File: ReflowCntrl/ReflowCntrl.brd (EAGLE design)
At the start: 86 x 50.8 mm, 13 parts, among them J1 DCJ0202, T1 2N2222, X1 1751248

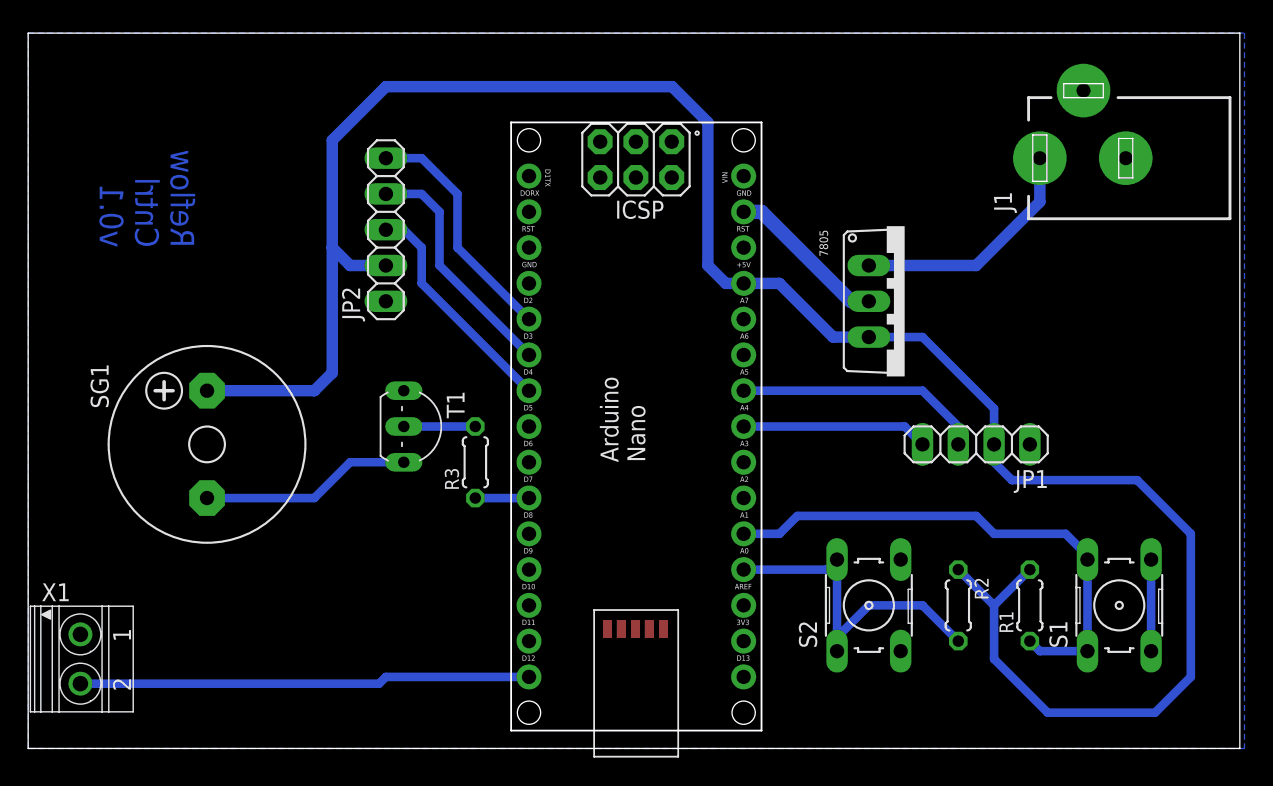
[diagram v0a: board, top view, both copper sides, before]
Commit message: Changed dimension boundry in Arduino Nano library to be tPlace instead to allow gnd plane to flow properly.
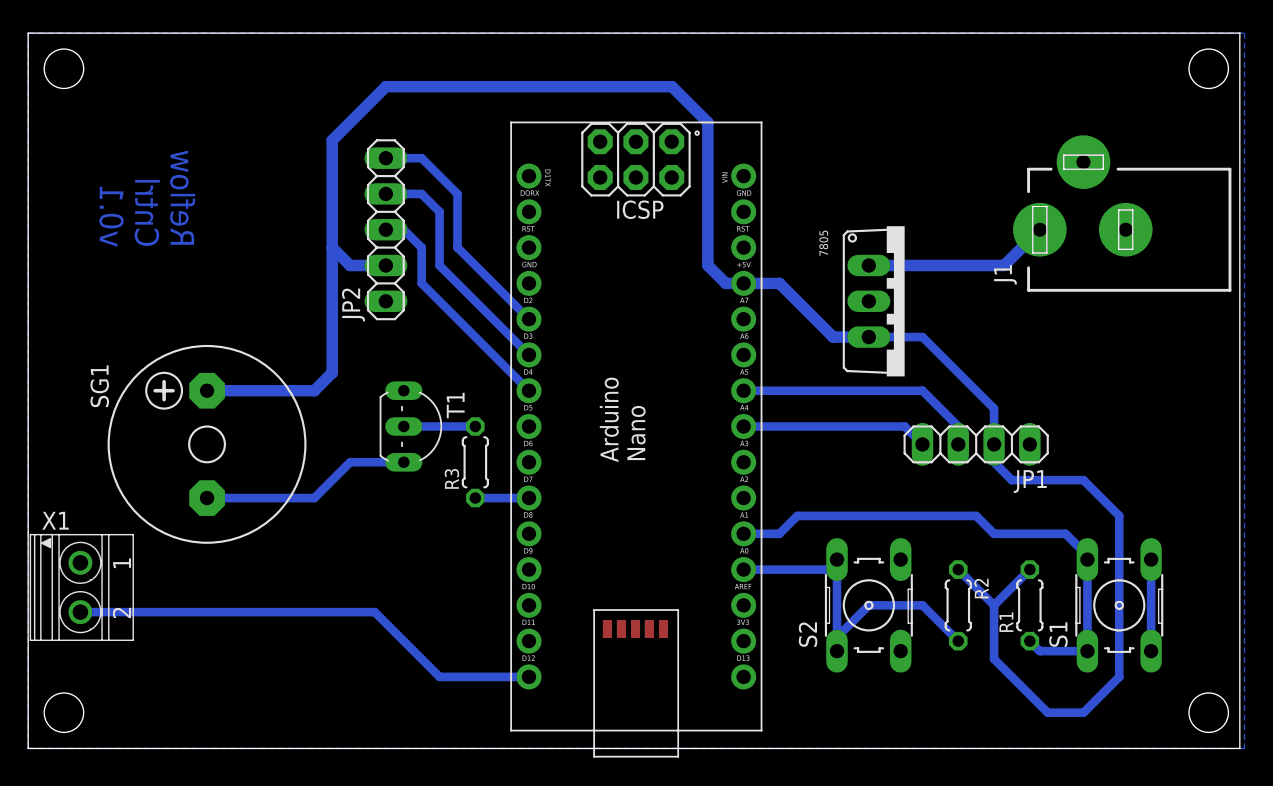
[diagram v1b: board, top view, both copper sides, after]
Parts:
- moved X1 5.08 mm to (3.81, 11.4)
- moved J1 5.08 mm to (74.9, 36.8)
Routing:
- net GND: track 18.0 -> 6.50 mm
- net VCC: track 151.9 -> 142.5 mm
- net N$5: track 17.1 -> 13.2 mm
- net SSR: track 32.0 -> 33.8 mm

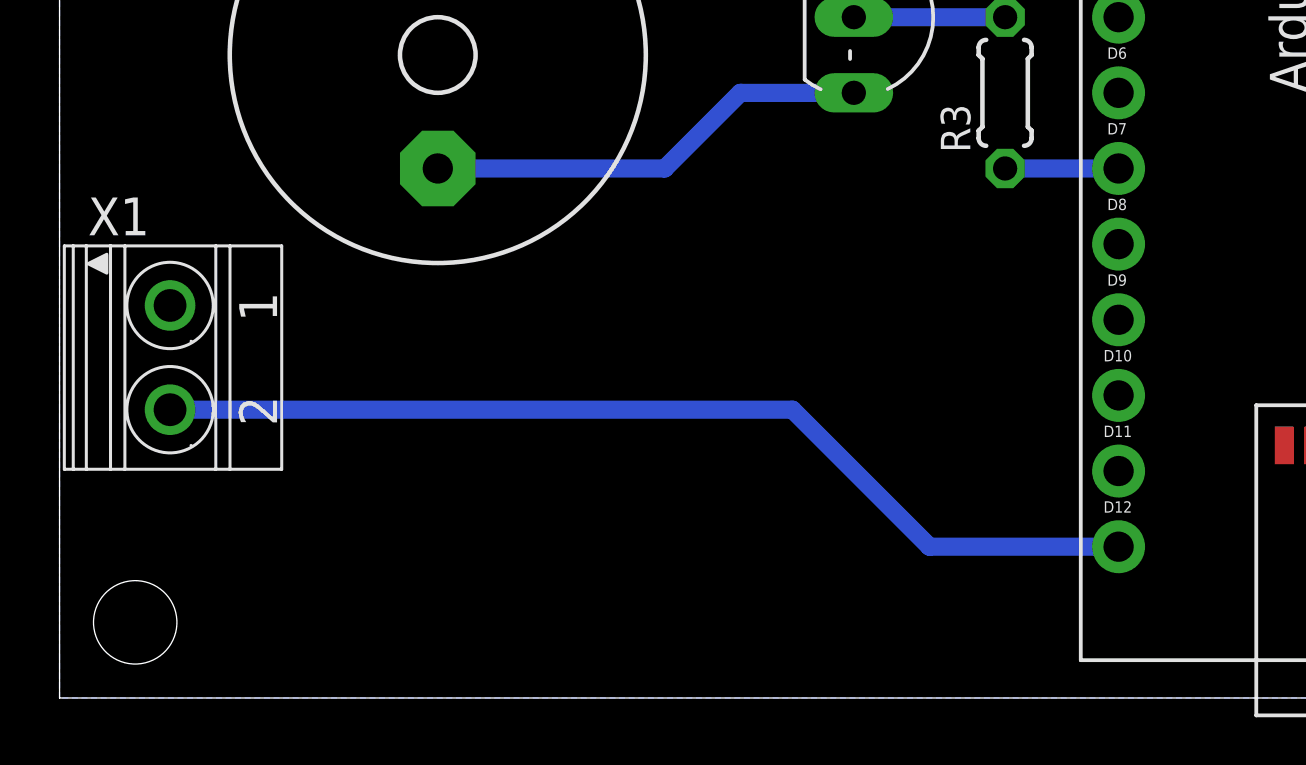
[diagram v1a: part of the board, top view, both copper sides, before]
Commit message: Change SSR terminal to Wago part.
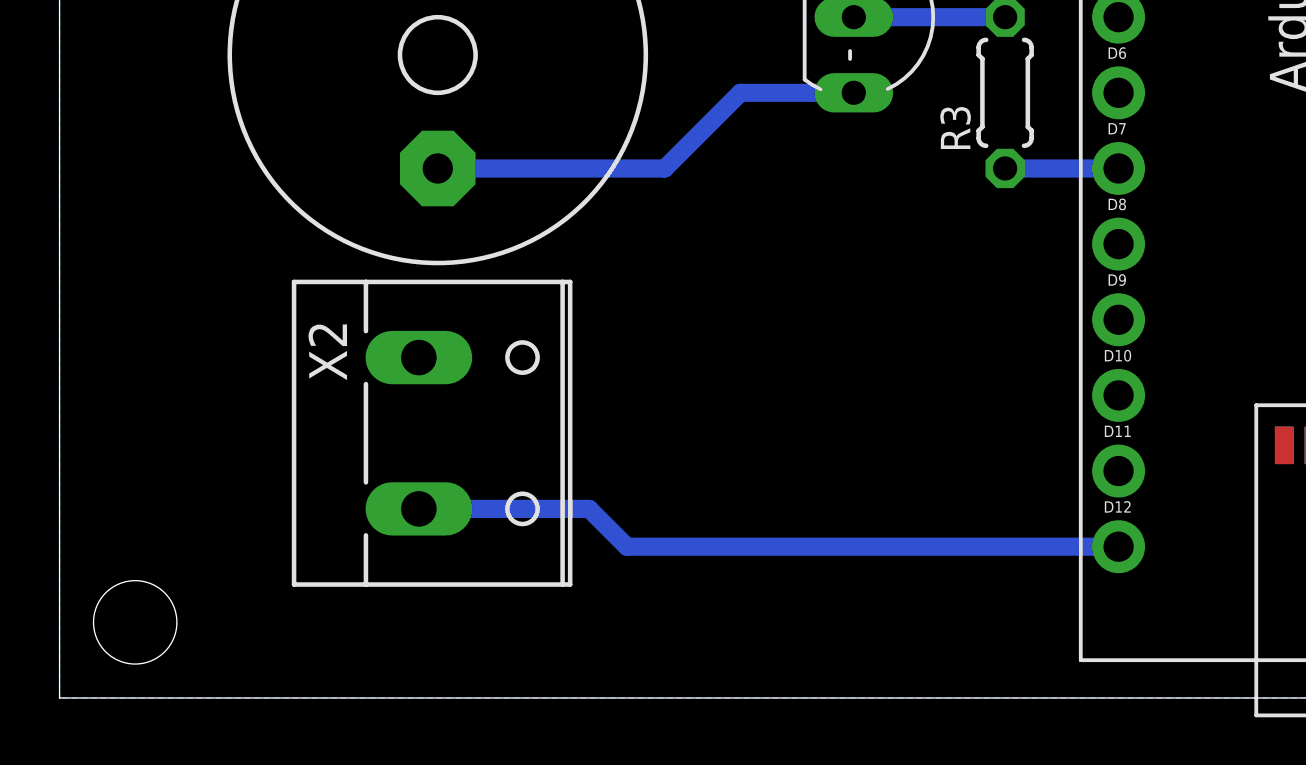
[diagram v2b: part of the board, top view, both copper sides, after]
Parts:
- removed X1: 1751248, con-phoenix-350:1751248
- added X2: (no value), con-wago-508:W237-132
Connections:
- net GND: now also X2.1; no longer X1.1
- net SSR: now also X2.2; no longer X1.2
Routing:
- net SSR: track 33.8 -> 24.0 mm

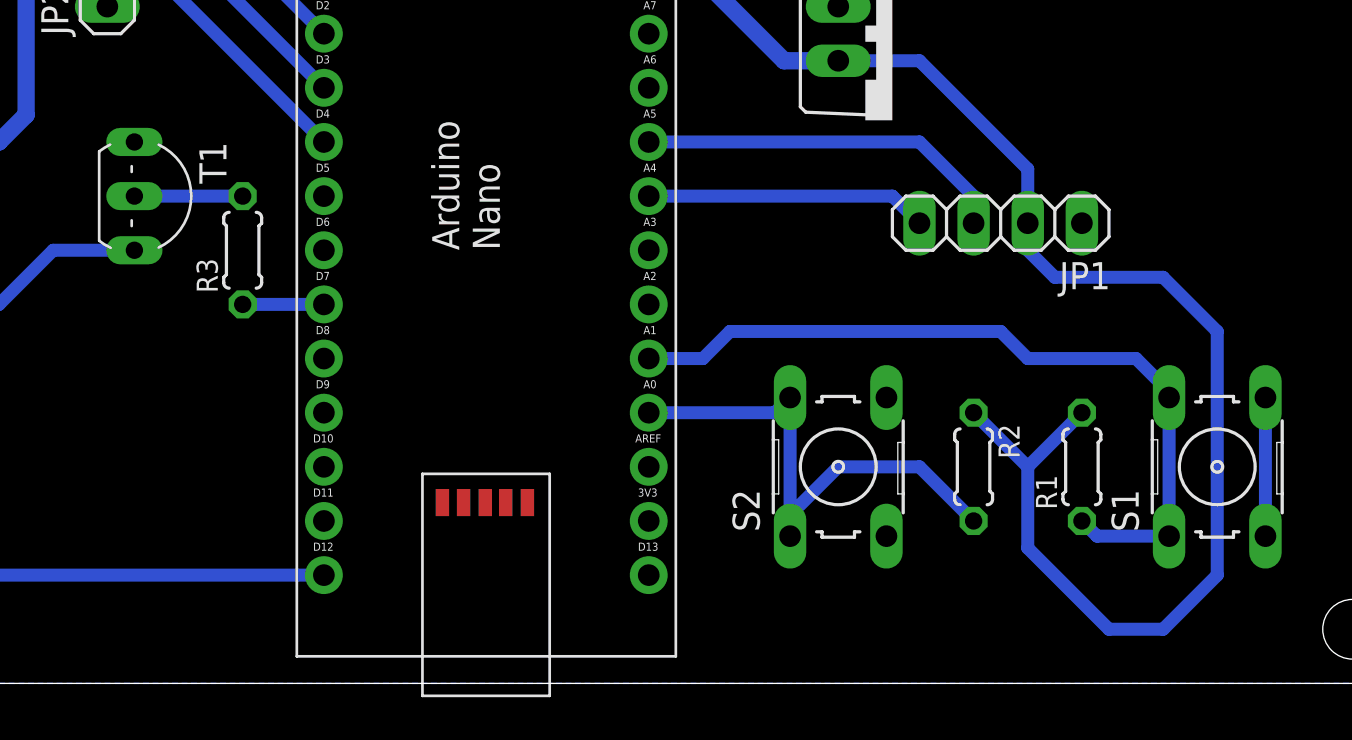
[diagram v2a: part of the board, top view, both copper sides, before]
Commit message: Change resistors to 0207/10 package
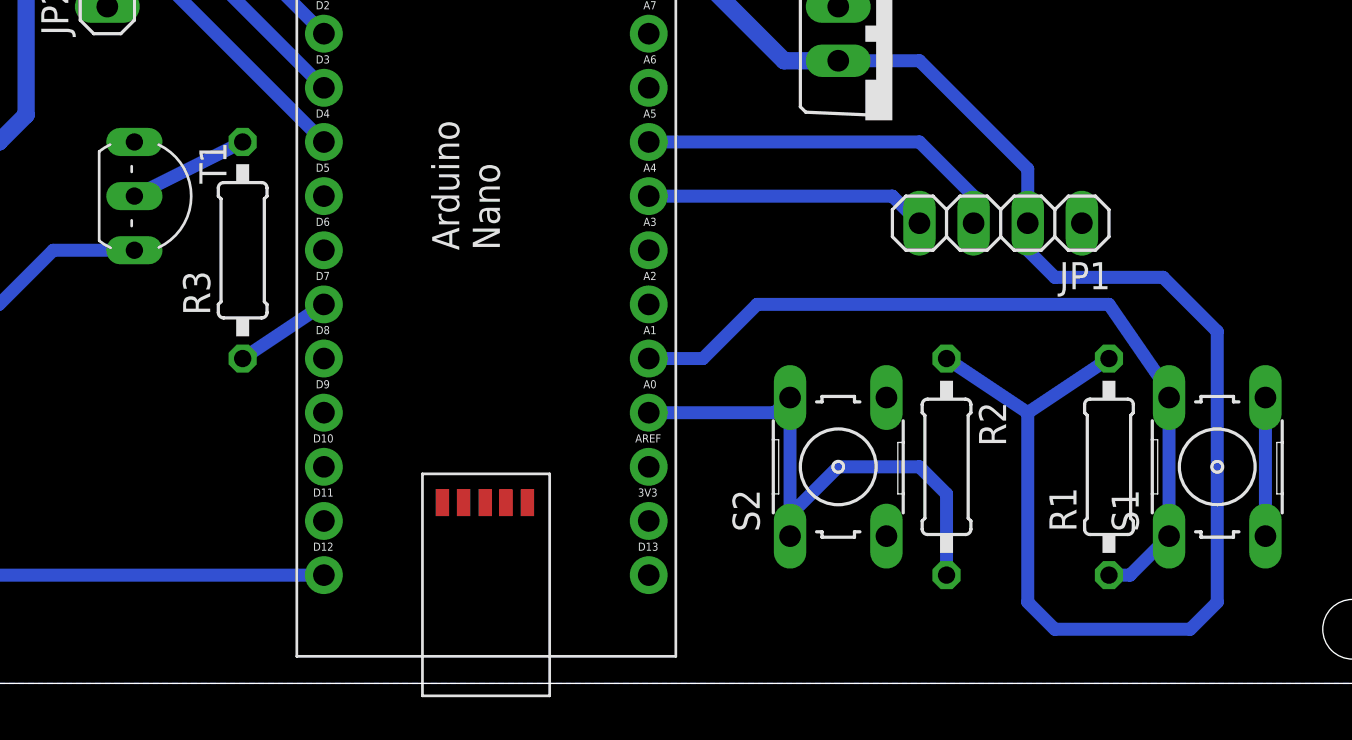
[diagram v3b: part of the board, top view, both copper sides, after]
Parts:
- R1, R2, R3: device rcl:0204/5 -> rcl:0207/10
- moved R2 1.27 mm to (64.8, 10.2)
- moved R1 1.27 mm to (72.4, 10.2)
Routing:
- net VCC: track 142.5 -> 149.2 mm
- net B1: track 25.0 -> 27.0 mm
- net BUZ: track 3.81 -> 4.58 mm
- net B0: track 37.3 -> 38.0 mm
- net N$2: track 5.08 -> 5.68 mm
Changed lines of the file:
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@@
 <element name="JP2" library="pinhead" package="1X05" value="Thermo" x="25.4" y="36.83" rot="R90"/>
 <element name="PCB1" library="E14_Arduino_revC" package="ARDUINO_NANO" value="ARDUINO_NANO" x="52.07" y="1.27" rot="R90"/>
-<element name="R1" library="rcl" package="0204/5" value="" x="71.12" y="10.16" rot="R90"/>
-<element name="R2" library="rcl" package="0204/5" value="" x="66.04" y="10.16" rot="R270"/>
-<element name="R3" library="rcl" package="0204/5" value="" x="31.75" y="20.32" rot="R90"/>
+<element name="R1" library="rcl" package="0207/10" value="" x="72.39" y="10.16" rot="R90"/>
+<element name="R2" library="rcl" package="0207/10" value="" x="64.77" y="10.16" rot="R270"/>
+<element name="R3" library="rcl" package="0207/10" value="" x="31.75" y="20.32" rot="R90"/>
 <element name="S1" library="switch-omron" package="B3F-10XX" value="" x="77.47" y="10.16" rot="R90">
 <attribute name="MPN" value="B3F-1000" x="77.47" y="10.16" size="1.778" layer="27" rot="R90" display="off"/>
@@
 <contactref element="R3" pad="2"/>
 <contactref element="T1" pad="B"/>
-<wire x1="31.75" y1="22.86" x2="26.67" y2="22.86" width="0.6096" layer="16"/>
+<wire x1="31.75" y1="25.4" x2="26.67" y2="22.86" width="0.6096" layer="16"/>
 </signal>
 <signal name="GND">
@@
 <contactref element="JP1" pad="1"/>
 <contactref element="X2" pad="1"/>
-<wire x1="61.9506" y1="13.4112" x2="61.9506" y2="6.9088" width="0" layer="19" extent="1-1"/>
 </signal>
 <signal name="VCC">
@@
 <wire x1="53.34" y1="33.02" x2="57.15" y2="29.21" width="0.8128" layer="16"/>
 <wire x1="57.15" y1="29.21" x2="59.69" y2="29.21" width="0.8128" layer="16"/>
-<wire x1="72.39" y1="2.54" x2="68.58" y2="6.35" width="0.6096" layer="16"/>
-<wire x1="68.58" y1="6.35" x2="68.58" y2="10.16" width="0.6096" layer="16"/>
-<wire x1="68.58" y1="10.16" x2="66.04" y2="12.7" width="0.6096" layer="16"/>
-<wire x1="71.12" y1="12.7" x2="68.58" y2="10.16" width="0.6096" layer="16"/>
+<wire x1="69.85" y1="2.54" x2="68.58" y2="3.81" width="0.6096" layer="16"/>
+<wire x1="68.58" y1="3.81" x2="68.58" y2="12.7" width="0.6096" layer="16"/>
+<wire x1="68.58" y1="12.7" x2="64.77" y2="15.24" width="0.6096" layer="16"/>
+<wire x1="72.39" y1="15.24" x2="68.58" y2="12.7" width="0.6096" layer="16"/>
 <contactref element="JP1" pad="2"/>
 <wire x1="59.69" y1="29.21" x2="63.5" y2="29.21" width="0.6096" layer="16"/>
@@
 <wire x1="69.85" y1="19.05" x2="74.93" y2="19.05" width="0.6096" layer="16"/>
 <wire x1="74.93" y1="19.05" x2="77.47" y2="16.51" width="0.6096" layer="16"/>
-<wire x1="77.47" y1="16.51" x2="77.47" y2="5.08" width="0.6096" layer="16"/>
-<wire x1="77.47" y1="5.08" x2="74.93" y2="2.54" width="0.6096" layer="16"/>
-<wire x1="74.93" y1="2.54" x2="72.39" y2="2.54" width="0.6096" layer="16"/>
+<wire x1="77.47" y1="16.51" x2="77.47" y2="3.81" width="0.6096" layer="16"/>
+<wire x1="77.47" y1="3.81" x2="76.2" y2="2.54" width="0.6096" layer="16"/>
+<wire x1="76.2" y1="2.54" x2="69.85" y2="2.54" width="0.6096" layer="16"/>
 </signal>
 <signal name="N$5">
@@
 <contactref element="PCB1" pad="A1"/>
 <wire x1="50.8" y1="15.24" x2="53.34" y2="15.24" width="0.6096" layer="16"/>
-<wire x1="53.34" y1="15.24" x2="54.61" y2="16.51" width="0.6096" layer="16"/>
-<wire x1="54.61" y1="16.51" x2="67.31" y2="16.51" width="0.6096" layer="16"/>
+<wire x1="53.34" y1="15.24" x2="55.88" y2="17.78" width="0.6096" layer="16"/>
+<wire x1="55.88" y1="17.78" x2="72.39" y2="17.78" width="0.6096" layer="16"/>
 <wire x1="75.2094" y1="6.9088" x2="75.2094" y2="13.4112" width="0.6096" layer="16"/>
-<wire x1="67.31" y1="16.51" x2="68.58" y2="15.24" width="0.6096" layer="16"/>
-<wire x1="68.58" y1="15.24" x2="73.66" y2="15.24" width="0.6096" layer="16"/>
-<wire x1="73.66" y1="15.24" x2="75.2094" y2="13.6906" width="0.6096" layer="16"/>
+<wire x1="72.39" y1="17.78" x2="75.2094" y2="13.6906" width="0.6096" layer="16"/>
 <wire x1="75.2094" y1="13.6906" x2="75.2094" y2="13.4112" width="0.6096" layer="16"/>
-<wire x1="71.12" y1="7.62" x2="71.8312" y2="6.9088" width="0.6096" layer="16"/>
-<wire x1="71.8312" y1="6.9088" x2="75.2094" y2="6.9088" width="0.6096" layer="16"/>
+<wire x1="72.39" y1="5.08" x2="73.3806" y2="5.08" width="0.6096" layer="16"/>
+<wire x1="73.3806" y1="5.08" x2="75.2094" y2="6.9088" width="0.6096" layer="16"/>
 </signal>
 <signal name="B1">
@@
 <wire x1="50.8" y1="12.7" x2="56.7182" y2="12.7" width="0.6096" layer="16"/>
 <wire x1="56.7182" y1="12.7" x2="57.4294" y2="13.4112" width="0.6096" layer="16"/>
-<wire x1="66.04" y1="7.62" x2="63.5" y2="10.16" width="0.6096" layer="16"/>
 <wire x1="63.5" y1="10.16" x2="59.69" y2="10.16" width="0.6096" layer="16"/>
 <wire x1="59.69" y1="10.16" x2="57.4294" y2="7.8994" width="0.6096" layer="16"/>
 <wire x1="57.4294" y1="7.8994" x2="57.4294" y2="6.9088" width="0.6096" layer="16"/>
+<wire x1="63.5" y1="10.16" x2="64.77" y2="8.89" width="0.6096" layer="16"/>
+<wire x1="64.77" y1="8.89" x2="64.77" y2="5.08" width="0.6096" layer="16"/>
 </signal>
 <signal name="SCK">
@@
 <contactref element="R3" pad="1"/>
 <contactref element="PCB1" pad="D7"/>
-<wire x1="31.75" y1="17.78" x2="35.56" y2="17.78" width="0.6096" layer="16"/>
+<wire x1="31.75" y1="15.24" x2="35.56" y2="17.78" width="0.6096" layer="16"/>
 </signal>
 <signal name="SSR">
